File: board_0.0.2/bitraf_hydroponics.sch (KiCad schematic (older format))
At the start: 32 parts, among them P1 12V_PWR, P10 ROT_BTN, P11 BUZZ, P12 LDR, P13 MOS_OUT_2, P14 MOS_OUT_1, P15 MOS_OUT_3, P17 BREAKOUT_1-15, P18 BREAKOUT_16-30, P2 I2C_1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

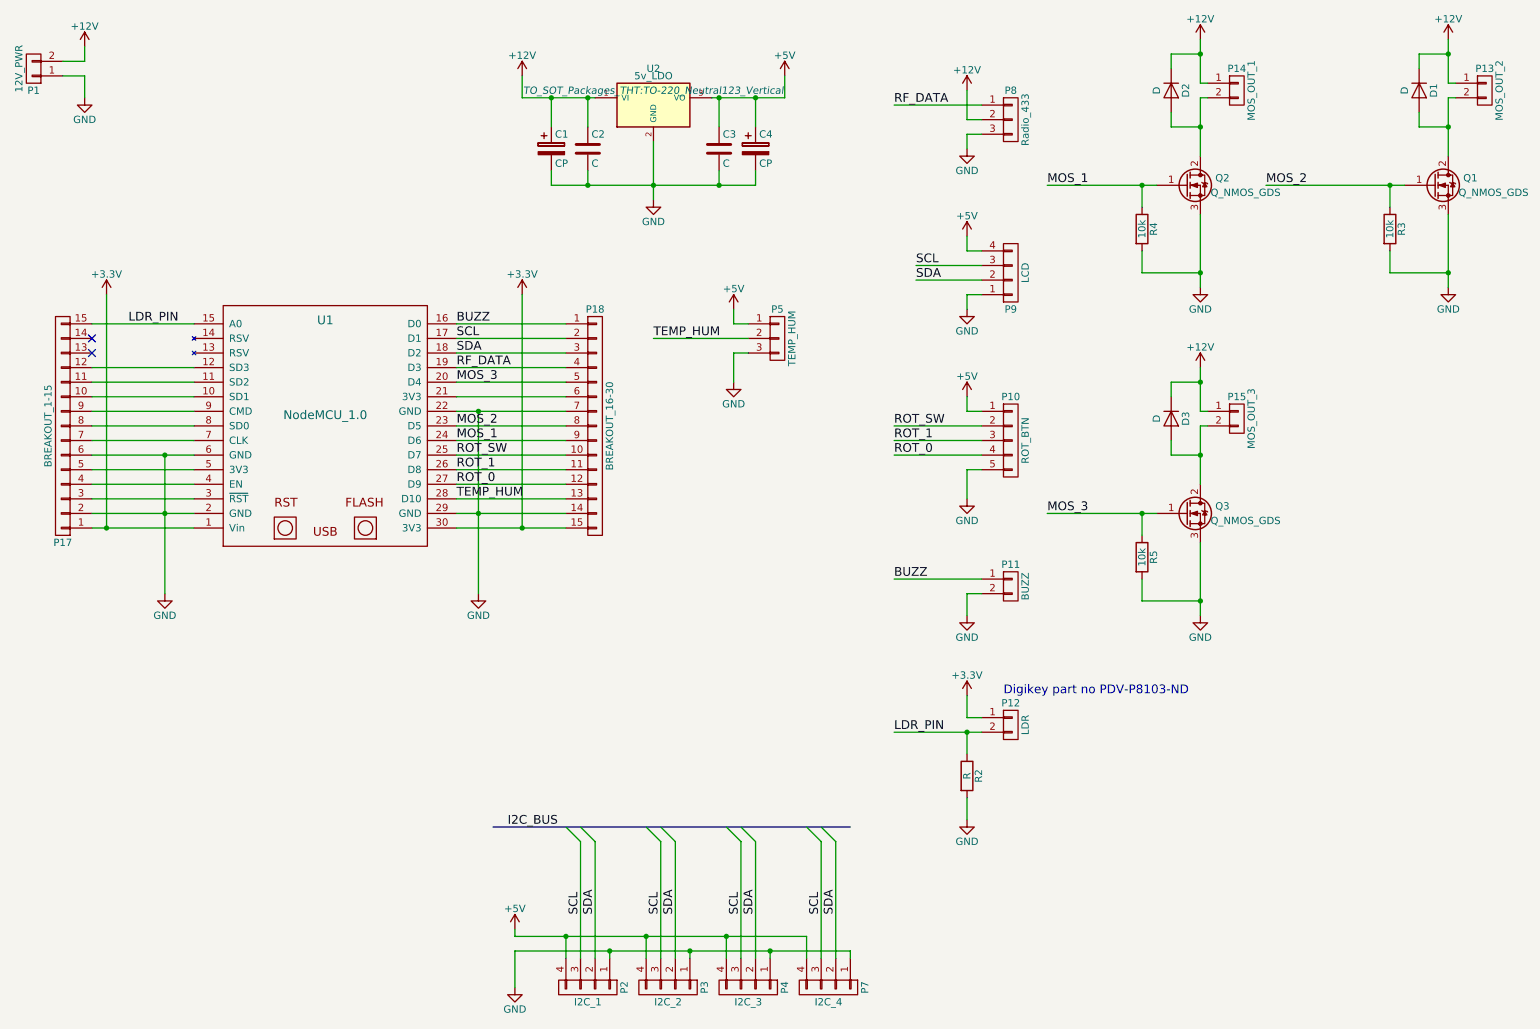
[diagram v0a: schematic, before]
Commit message: fixed Vin bug. Traced new route for buzz and ldr. Added resistors to terminals
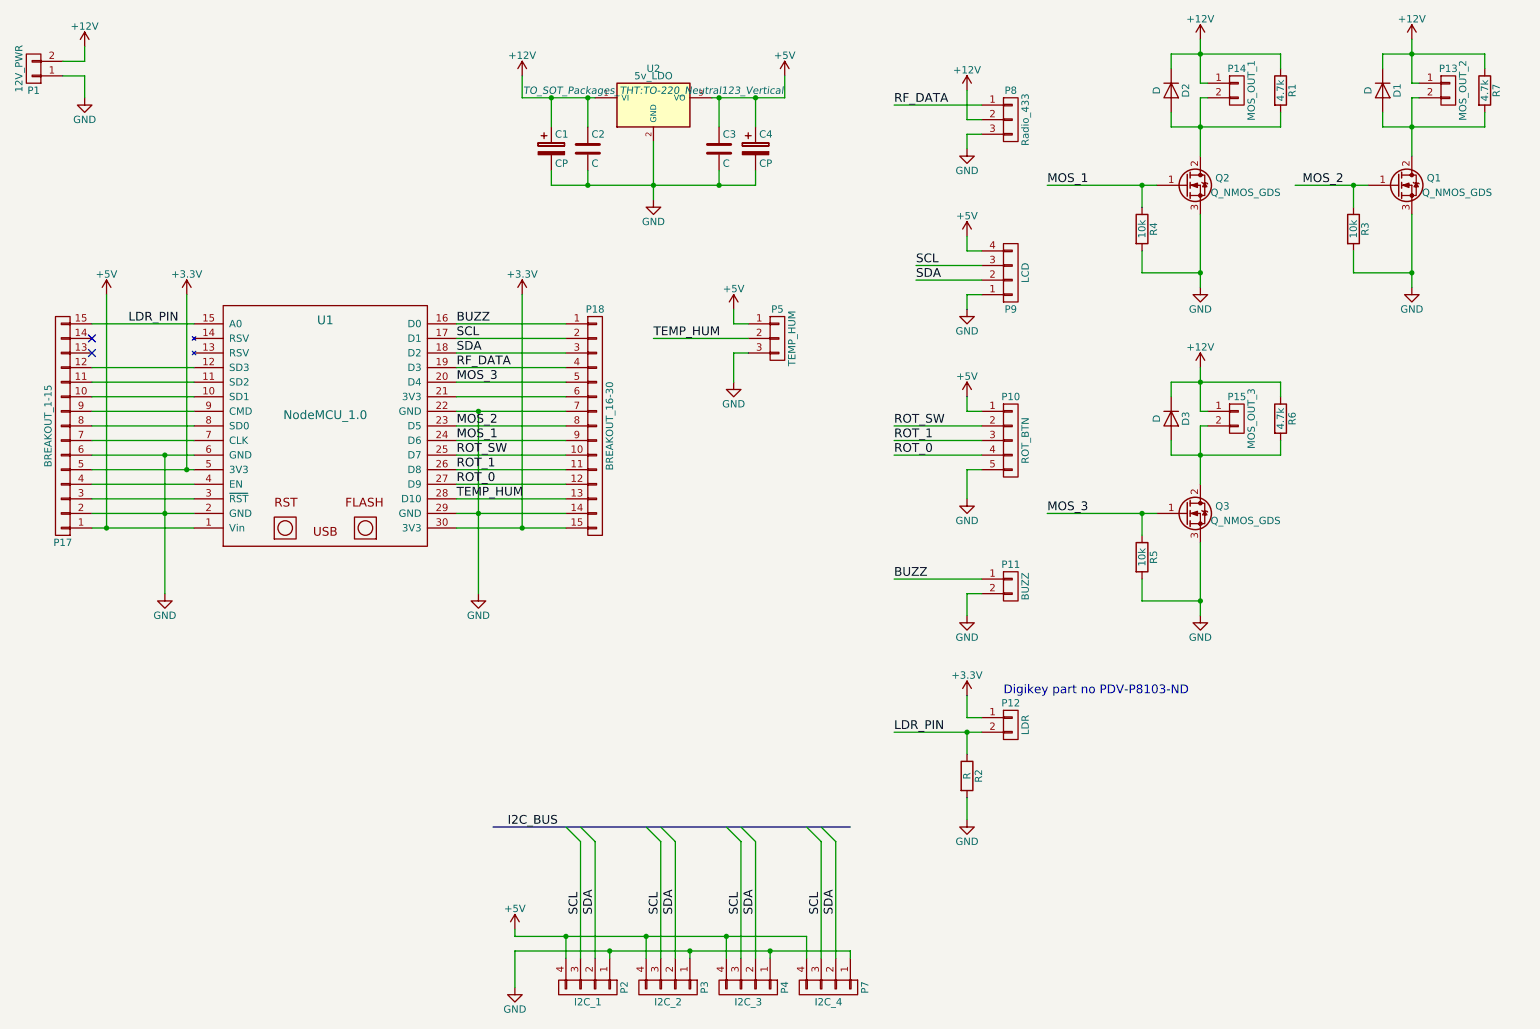
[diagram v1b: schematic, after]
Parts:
- added R1, R6, R7: 4.7k, Resistors_ThroughHole:Resistor_Horizontal_RM10mm, symbol R
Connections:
- net +12V: now also R1.1, R6.1, R7.1
- net +3V3: now also P17.5 (P5), U1.5 (3V3); no longer P17.1 (P1), U1.1 (Vin)
- net +5V: now also P17.1 (P1), U1.1 (Vin)
- net at D2.2 (A), P14.2 (P2), Q2.2 (D): now also R1.2
- net at D1.2 (A), P13.2 (P2), Q1.2 (D): now also R7.2
- net at D3.2 (A), P15.2 (P2), Q3.2 (D): now also R6.2
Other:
- moved on the sheet: D1, P13, Q1, R3

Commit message: moved i2c bus out of the way for USB and rerouted. Also removed resistors over terminals
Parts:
- removed R1, R6, R7: 4.7k, Resistors_ThroughHole:Resistor_Horizontal_RM10mm, symbol R
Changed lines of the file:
@@
 $EndComp
 $Comp
-L +12V #PWR24
+L +12V #PWR01
 U 1 1 57E43918
 P 9100 900
-F 0 "#PWR24" H 9100 750 50  0001 C CNN
+F 0 "#PWR01" H 9100 750 50  0001 C CNN
 F 1 "+12V" H 9100 1040 50  0000 C CNN
 F 2 "" H 9100 900 50  0000 C CNN
@@
 $EndComp
 $Comp
-L GND #PWR25
+L GND #PWR02
 U 1 1 57E43A4F
 P 9100 2600
-F 0 "#PWR25" H 9100 2350 50  0001 C CNN
+F 0 "#PWR02" H 9100 2350 50  0001 C CNN
 F 1 "GND" H 9100 2450 50  0000 C CNN
 F 2 "" H 9100 2600 50  0000 C CNN
@@
 $EndComp
 $Comp
-L +12V #PWR28
+L +12V #PWR03
 U 1 1 57E44263
 P 10550 900
-F 0 "#PWR28" H 10550 750 50  0001 C CNN
+F 0 "#PWR03" H 10550 750 50  0001 C CNN
 F 1 "+12V" H 10550 1040 50  0000 C CNN
 F 2 "" H 10550 900 50  0000 C CNN
@@
 $EndComp
 $Comp
-L GND #PWR29
+L GND #PWR04
 U 1 1 57E44275
 P 10550 2600
-F 0 "#PWR29" H 10550 2350 50  0001 C CNN
+F 0 "#PWR04" H 10550 2350 50  0001 C CNN
 F 1 "GND" H 10550 2450 50  0000 C CNN
 F 2 "" H 10550 2600 50  0000 C CNN
@@
 $EndComp
 $Comp
-L +12V #PWR26
+L +12V #PWR05
 U 1 1 57E4441E
 P 9100 3150
-F 0 "#PWR26" H 9100 3000 50  0001 C CNN
+F 0 "#PWR05" H 9100 3000 50  0001 C CNN
 F 1 "+12V" H 9100 3290 50  0000 C CNN
 F 2 "" H 9100 3150 50  0000 C CNN
@@
 $EndComp
 $Comp
-L GND #PWR27
+L GND #PWR06
 U 1 1 57E44430
 P 9100 4850
-F 0 "#PWR27" H 9100 4600 50  0001 C CNN
+F 0 "#PWR06" H 9100 4600 50  0001 C CNN
 F 1 "GND" H 9100 4700 50  0000 C CNN
 F 2 "" H 9100 4850 50  0000 C CNN
@@
 $EndComp
 $Comp
-L +12V #PWR15
+L +12V #PWR07
 U 1 1 57E4473A
 P 7500 1250
-F 0 "#PWR15" H 7500 1100 50  0001 C CNN
+F 0 "#PWR07" H 7500 1100 50  0001 C CNN
 F 1 "+12V" H 7500 1390 50  0000 C CNN
 F 2 "" H 7500 1250 50  0000 C CNN
@@
 $EndComp
 $Comp
-L GND #PWR16
+L GND #PWR08
 U 1 1 57E448A5
 P 7500 1650
-F 0 "#PWR16" H 7500 1400 50  0001 C CNN
+F 0 "#PWR08" H 7500 1400 50  0001 C CNN
 F 1 "GND" H 7500 1500 50  0000 C CNN
 F 2 "" H 7500 1650 50  0000 C CNN
@@
 $EndComp
 $Comp
-L GND #PWR18
+L GND #PWR09
 U 1 1 57E44B00
 P 7500 2750
-F 0 "#PWR18" H 7500 2500 50  0001 C CNN
+F 0 "#PWR09" H 7500 2500 50  0001 C CNN
 F 1 "GND" H 7500 2600 50  0000 C CNN
 F 2 "" H 7500 2750 50  0000 C CNN
@@
 $EndComp
 $Comp
-L GND #PWR20
+L GND #PWR010
 U 1 1 57E44E67
 P 7500 4050
-F 0 "#PWR20" H 7500 3800 50  0001 C CNN
+F 0 "#PWR010" H 7500 3800 50  0001 C CNN
 F 1 "GND" H 7500 3900 50  0000 C CNN
 F 2 "" H 7500 4050 50  0000 C CNN
@@
 $EndComp
 $Comp
-L +5V #PWR19
+L +5V #PWR011
 U 1 1 57E44EEE
 P 7500 3350
-F 0 "#PWR19" H 7500 3200 50  0001 C CNN
+F 0 "#PWR011" H 7500 3200 50  0001 C CNN
 F 1 "+5V" H 7500 3490 50  0000 C CNN
 F 2 "" H 7500 3350 50  0000 C CNN
@@
 $EndComp
 $Comp
-L +12V #PWR9
+L +12V #PWR012
 U 1 1 57E45256
 P 4450 1150
-F 0 "#PWR9" H 4450 1000 50  0001 C CNN
+F 0 "#PWR012" H 4450 1000 50  0001 C CNN
 F 1 "+12V" H 4450 1290 50  0000 C CNN
 F 2 "" H 4450 1150 50  0000 C CNN
@@
 $EndComp
 $Comp
-L +5V #PWR14
+L +5V #PWR013
 U 1 1 57E452E7
 P 6250 1150
-F 0 "#PWR14" H 6250 1000 50  0001 C CNN
+F 0 "#PWR013" H 6250 1000 50  0001 C CNN
 F 1 "+5V" H 6250 1290 50  0000 C CNN
 F 2 "" H 6250 1150 50  0000 C CNN
@@
 $EndComp
 $Comp
-L GND #PWR11
+L GND #PWR014
 U 1 1 57E453D6
 P 5350 2000
-F 0 "#PWR11" H 5350 1750 50  0001 C CNN
+F 0 "#PWR014" H 5350 1750 50  0001 C CNN
 F 1 "GND" H 5350 1850 50  0000 C CNN
 F 2 "" H 5350 2000 50  0000 C CNN
@@
 Wire Wire Line
 	8900 1400 8900 1500
-Wire Wire Line
-	8900 1500 9650 1500
 Connection ~ 9100 1500
 Wire Wire Line
 	8900 1100 8900 1000
-Wire Wire Line
-	8900 1000 9650 1000
 Connection ~ 9100 1000
 Wire Wire Line
@@
 Wire Wire Line
 	10350 1400 10350 1500
-Wire Wire Line
-	10350 1500 11050 1500
 Connection ~ 10550 1500
 Wire Wire Line
 	10350 1100 10350 1000
-Wire Wire Line
-	10350 1000 11050 1000
 Connection ~ 10550 1000
 Wire Wire Line
@@
 	8900 3650 8900 3750
 Wire Wire Line
-	8900 3750 9650 3750
-Connection ~ 9100 3750
-Wire Wire Line
 	8900 3350 8900 3250
-Wire Wire Line
-	8900 3250 9650 3250
-Connection ~ 9100 3250
 Wire Wire Line
 	9100 4350 9100 4850
@@
 	1450 1050 1450 950
 $Comp
-L +12V #PWR1
+L +12V #PWR015
 U 1 1 57E46BD8
 P 1450 950
-F 0 "#PWR1" H 1450 800 50  0001 C CNN
+F 0 "#PWR015" H 1450 800 50  0001 C CNN
 F 1 "+12V" H 1450 1090 50  0000 C CNN
 F 2 "" H 1450 950 50  0000 C CNN
@@
 	1450 1150 1450 1300
 $Comp
-L GND #PWR2
+L GND #PWR016
 U 1 1 57E46C8D
 P 1450 1300
-F 0 "#PWR2" H 1450 1050 50  0001 C CNN
+F 0 "#PWR016" H 1450 1050 50  0001 C CNN
 F 1 "GND" H 1450 1150 50  0000 C CNN
 F 2 "" H 1450 1300 50  0000 C CNN
@@
 	7500 4700 7500 4850
 $Comp
-L GND #PWR21
+L GND #PWR017
 U 1 1 57E4803A
 P 7500 4850
-F 0 "#PWR21" H 7500 4600 50  0001 C CNN
+F 0 "#PWR017" H 7500 4600 50  0001 C CNN
 F 1 "GND" H 7500 4700 50  0000 C CNN
 F 2 "" H 7500 4850 50  0000 C CNN
@@
 	7500 6100 7500 6250
 $Comp
-L GND #PWR23
+L GND #PWR018
 U 1 1 57E49A14
 P 7500 6250
-F 0 "#PWR23" H 7500 6000 50  0001 C CNN
+F 0 "#PWR018" H 7500 6000 50  0001 C CNN
 F 1 "GND" H 7500 6100 50  0000 C CNN
 F 2 "" H 7500 6250 50  0000 C CNN
@@
 	7500 5550 7500 5400
 $Comp
-L +3.3V #PWR22
+L +3.3V #PWR019
 U 1 1 57E49FA4
 P 7500 5400
-F 0 "#PWR22" H 7500 5250 50  0001 C CNN
+F 0 "#PWR019" H 7500 5250 50  0001 C CNN
 F 1 "+3.3V" H 7500 5540 50  0000 C CNN
 F 2 "" H 7500 5400 50  0000 C CNN
@@
 	5900 2850 5900 2750
 $Comp
-L +5V #PWR12
+L +5V #PWR020
 U 1 1 57E4F4CB
 P 5900 2750
-F 0 "#PWR12" H 5900 2600 50  0001 C CNN
+F 0 "#PWR020" H 5900 2600 50  0001 C CNN
 F 1 "+5V" H 5900 2890 50  0000 C CNN
 F 2 "" H 5900 2750 50  0000 C CNN
@@
 	5900 3050 5900 3250
 $Comp
-L GND #PWR13
+L GND #PWR021
 U 1 1 57E4F67F
 P 5900 3250
-F 0 "#PWR13" H 5900 3000 50  0001 C CNN
+F 0 "#PWR021" H 5900 3000 50  0001 C CNN
 F 1 "GND" H 5900 3100 50  0000 C CNN
 F 2 "" H 5900 3250 50  0000 C CNN
@@
 	4400 7150 4400 7400
 $Comp
-L GND #PWR8
+L GND #PWR022
 U 1 1 57E53B7A
 P 4400 7400
-F 0 "#PWR8" H 4400 7150 50  0001 C CNN
+F 0 "#PWR022" H 4400 7150 50  0001 C CNN
 F 1 "GND" H 4400 7250 50  0000 C CNN
 F 2 "" H 4400 7400 50  0000 C CNN
@@
 $EndComp
 $Comp
-L +5V #PWR7
+L +5V #PWR023
 U 1 1 57E53BD0
 P 4400 7000
-F 0 "#PWR7" H 4400 6850 50  0001 C CNN
+F 0 "#PWR023" H 4400 6850 50  0001 C CNN
 F 1 "+5V" H 4400 7140 50  0000 C CNN
 F 2 "" H 4400 7000 50  0000 C CNN
@@
 	2000 3750 2000 4700
 $Comp
-L GND #PWR4
+L GND #PWR024
 U 1 1 57E579BA
 P 2000 4700
-F 0 "#PWR4" H 2000 4450 50  0001 C CNN
+F 0 "#PWR024" H 2000 4450 50  0001 C CNN
 F 1 "GND" H 2000 4550 50  0000 C CNN
 F 2 "" H 2000 4700 50  0000 C CNN
@@
 $EndComp
 $Comp
-L GND #PWR6
+L GND #PWR025
 U 1 1 57E57A2F
 P 4150 4700
-F 0 "#PWR6" H 4150 4450 50  0001 C CNN
+F 0 "#PWR025" H 4150 4450 50  0001 C CNN
 F 1 "GND" H 4150 4550 50  0000 C CNN
 F 2 "" H 4150 4700 50  0000 C CNN
@@
 	4000 4250 4750 4250
 $Comp
-L +3.3V #PWR10
+L +3.3V #PWR026
 U 1 1 57E5A8F3
 P 4450 2650
-F 0 "#PWR10" H 4450 2500 50  0001 C CNN
+F 0 "#PWR026" H 4450 2500 50  0001 C CNN
 F 1 "+3.3V" H 4450 2790 50  0000 C CNN
 F 2 "" H 4450 2650 50  0000 C CNN
@@
 	4000 2850 4750 2850
 $Comp
-L +5V #PWR17
+L +5V #PWR027
 U 1 1 57ED6C9F
 P 7500 2250
-F 0 "#PWR17" H 7500 2100 50  0001 C CNN
+F 0 "#PWR027" H 7500 2100 50  0001 C CNN
 F 1 "+5V" H 7500 2390 50  0000 C CNN
 F 2 "" H 7500 2250 50  0000 C CNN
@@
 	1600 4250 1600 2650
 $Comp
-L +5V #PWR3
+L +5V #PWR028
 U 1 1 58780D74
 P 1600 2650
-F 0 "#PWR3" H 1600 2500 50  0001 C CNN
+F 0 "#PWR028" H 1600 2500 50  0001 C CNN
 F 1 "+5V" H 1600 2790 50  0000 C CNN
 F 2 "" H 1600 2650 50  0000 C CNN
@@
 Connection ~ 2150 3850
 $Comp
-L +3.3V #PWR5
+L +3.3V #PWR029
 U 1 1 58780FF6
 P 2150 2650
-F 0 "#PWR5" H 2150 2500 50  0001 C CNN
+F 0 "#PWR029" H 2150 2500 50  0001 C CNN
 F 1 "+3.3V" H 2150 2790 50  0000 C CNN
 F 2 "" H 2150 2650 50  0000 C CNN
@@
 	1    0    0    -1
 $EndComp
-$Comp
-L R R6
-U 1 1 587841A7
-P 9650 3500
-F 0 "R6" V 9730 3500 50  0000 C CNN
-F 1 "4.7k" V 9650 3500 50  0000 C CNN
-F 2 "Resistors_ThroughHole:Resistor_Horizontal_RM10mm" V 9580 3500 50  0001 C CNN
-F 3 "" H 9650 3500 50  0000 C CNN
-	1    9650 3500
-	1    0    0    -1
-$EndComp
-Wire Wire Line
-	9650 3250 9650 3350
-Wire Wire Line
-	9650 3750 9650 3650
-$Comp
-L R R1
-U 1 1 58785155
-P 9650 1250
-F 0 "R1" V 9730 1250 50  0000 C CNN
-F 1 "4.7k" V 9650 1250 50  0000 C CNN
-F 2 "Resistors_ThroughHole:Resistor_Horizontal_RM10mm" V 9580 1250 50  0001 C CNN
-F 3 "" H 9650 1250 50  0000 C CNN
-	1    9650 1250
-	1    0    0    -1
-$EndComp
-Wire Wire Line
-	9650 1000 9650 1100
-Wire Wire Line
-	9650 1500 9650 1400
-$Comp
-L R R7
-U 1 1 587854C0
-P 11050 1250
-F 0 "R7" V 11130 1250 50  0000 C CNN
-F 1 "4.7k" V 11050 1250 50  0000 C CNN
-F 2 "Resistors_ThroughHole:Resistor_Horizontal_RM10mm" V 10980 1250 50  0001 C CNN
-F 3 "" H 11050 1250 50  0000 C CNN
-	1    11050 1250
-	1    0    0    -1
-$EndComp
-Wire Wire Line
-	11050 1000 11050 1100
-Wire Wire Line
-	11050 1500 11050 1400
+Connection ~ 9100 3750
+Connection ~ 9100 3250
+Wire Wire Line
+	8900 3250 9100 3250
+Wire Wire Line
+	8900 3750 9100 3750
+Wire Wire Line
+	8900 1000 9100 1000
+Wire Wire Line
+	8900 1500 9100 1500
+Wire Wire Line
+	10350 1000 10550 1000
+Wire Wire Line
+	10350 1500 10550 1500
 $EndSCHEMATC

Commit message: o Refreshing footprints with updated KiCAD libraries. All parts have 3D-models now except the NodeMCU. o Adding some more text on the copper. o Fixing a couple of ERC warnings.
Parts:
- C1, C4: footprint Capacitors_ThroughHole:C_Radial_D5_L6_P2.5 -> Capacitors_THT:CP_Radial_D5.0mm_P2.50mm
- C2, C3: footprint Capacitors_ThroughHole:C_Disc_D3_P2.5 -> Capacitors_THT:C_Disc_D3.0mm_W2.0mm_P2.50mm
- D1, D2, D3: footprint Diodes_ThroughHole:Diode_DO-41_SOD81_Horizontal_RM10 -> Diodes_THT:D_DO-41_SOD81_P10.16mm_Horizontal
- P10: footprint Pin_Headers:Pin_Header_Straight_1x05 -> Pin_Headers:Pin_Header_Straight_1x05_Pitch2.54mm
- P11, P12: footprint Pin_Headers:Pin_Header_Straight_1x02 -> Pin_Headers:Pin_Header_Straight_1x02_Pitch2.54mm
- P17, P18: footprint Pin_Headers:Pin_Header_Straight_1x15 -> Pin_Headers:Pin_Header_Straight_1x15_Pitch2.54mm
- P2, P3, P4, P7, P9: footprint Pin_Headers:Pin_Header_Straight_1x04 -> Pin_Headers:Pin_Header_Straight_1x04_Pitch2.54mm
- P5, P8: footprint Pin_Headers:Pin_Header_Straight_1x03 -> Pin_Headers:Pin_Header_Straight_1x03_Pitch2.54mm
- Q1, Q2, Q3, U2: footprint TO_SOT_Packages_THT:TO-220_Neutral123_Vertical -> TO_SOT_Packages_THT:TO-220_Vertical
- R2, R3, R4, R5: footprint Resistors_ThroughHole:Resistor_Horizontal_RM10mm -> Resistors_THT:R_Axial_DIN0207_L6.3mm_D2.5mm_P10.16mm_Horizontal
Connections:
- net +3V3: now also P18.6 (P6), U1.21 (3V3)
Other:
- moved on the sheet: P17, P18, U1
